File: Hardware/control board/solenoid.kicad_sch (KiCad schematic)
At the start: 8 parts, among them J11 Screw_Terminal_01x02, Q3 NMOS

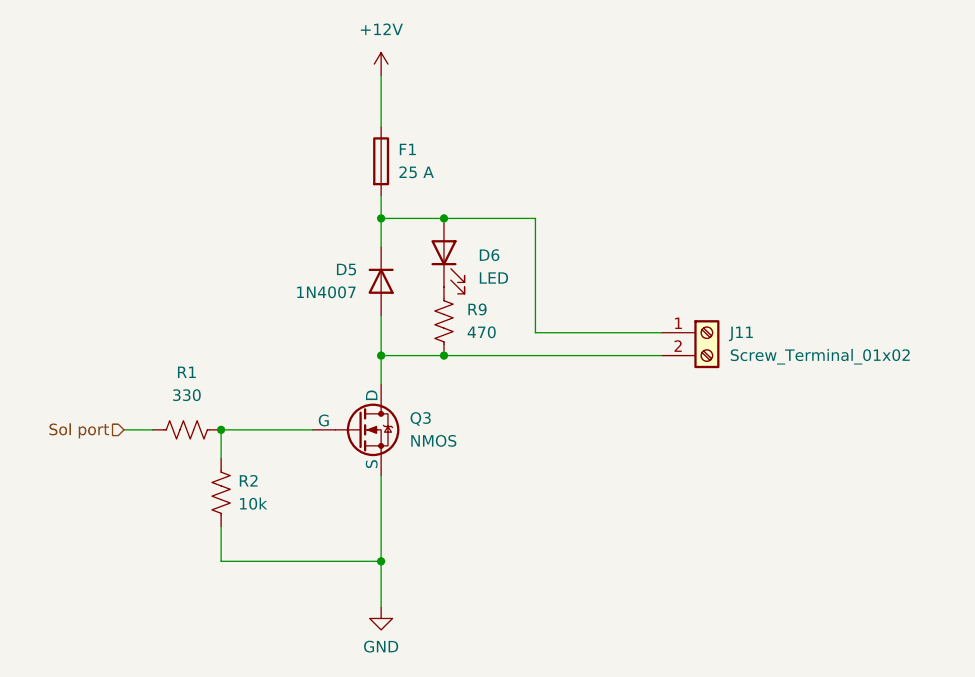
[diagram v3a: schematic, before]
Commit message: updated resistor values for 14.8 V battery
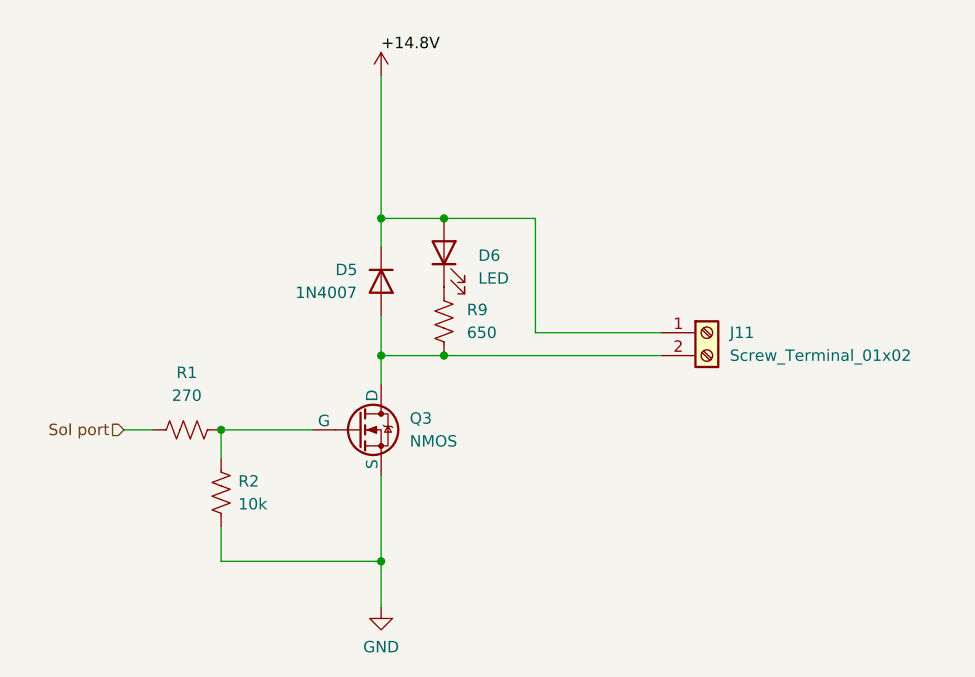
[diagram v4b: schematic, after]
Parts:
- removed F1: 25 A, symbol Device:Fuse
- R1: value 330 -> 270
- R9: value 470 -> 650
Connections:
- net +12V: now also D5.1 (K), D6.2 (A), J11.1 (Pin_1)
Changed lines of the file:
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@@
-    (stroke (width 0) (type default))
-  )
-  (wire (pts (xy 122.555 73.025) (xy 122.555 75.565))
     (stroke (width 0) (type default))
   )
@@
     (stroke (width 0) (type default))
   )
-  (wire (pts (xy 122.555 59.69) (xy 122.555 65.405))
+  (wire (pts (xy 122.555 59.69) (xy 122.555 75.565))
     (stroke (width 0) (type default))
   )
   (wire (pts (xy 139.7 88.265) (xy 153.67 88.265))
     (stroke (width 0) (type default))
+  )
+  (label "+14.8V" (at 122.555 57.15 0) (fields_autoplaced)
+    (effects (font (size 1.27 1.27)) (justify left bottom))
   )
   (hierarchical_label "Sol port" (shape input) (at 93.98 99.06 180) (fields_autoplaced)
@@
     )
   )
-  (symbol (lib_id "Device:Fuse") (at 122.555 69.215 0) (unit 1)
-    (in_bom yes) (on_board yes) (dnp no) (fields_autoplaced)
-    (property "Reference" "F1" (at 124.46 67.945 0)
-      (effects (font (size 1.27 1.27)) (justify left))
-    )
-    (property "Value" "25 A" (at 124.46 70.485 0)
-      (effects (font (size 1.27 1.27)) (justify left))
-    )
-    (property "Footprint" "" (at 120.777 69.215 90)
-      (effects (font (size 1.27 1.27)) hide)
-    )
-    (property "Datasheet" "~" (at 122.555 69.215 0)
-      (effects (font (size 1.27 1.27)) hide)
-    )
-    (pin "1")
-    (pin "2")
-    (instances
-      (project "solenoid"
-        (path "/b4ed5960-473e-41d7-9d87-eb439ed22219"
-          (reference "F1") (unit 1)
-        )
-      )
-      (project "control board"
-        (path "/cf0863a8-7f64-449b-8eb4-3c06c871fb37/9fd0b45f-6f46-40af-ae0d-29c33b45e498"
-          (reference "F1") (unit 1)
-        )
-        (path "/cf0863a8-7f64-449b-8eb4-3c06c871fb37/6163a064-c95f-47b6-9c17-0e18c391c233"
-          (reference "F1") (unit 1)
-        )
-        (path "/cf0863a8-7f64-449b-8eb4-3c06c871fb37/f39ce93b-3626-4dde-a021-b00a2c8134c7"
-          (reference "F1") (unit 1)
-        )
-      )
-    )
-  )
   (symbol (lib_id "Device:LED") (at 129.54 79.375 90) (unit 1)
     (in_bom yes) (on_board yes) (dnp no) (fields_autoplaced)
@@
       (effects (font (size 1.27 1.27)))
     )
-    (property "Value" "330" (at 100.965 95.25 90)
+    (property "Value" "270" (at 100.965 95.25 90)
       (effects (font (size 1.27 1.27)))
     )
@@
       (effects (font (size 1.27 1.27)) (justify left))
     )
-    (property "Value" "470" (at 132.08 88.265 0)
+    (property "Value" "650" (at 132.08 88.265 0)
       (effects (font (size 1.27 1.27)) (justify left))
     )
@@
   )
   (symbol (lib_id "power:+12V") (at 122.555 59.69 0) (unit 1)
-    (in_bom yes) (on_board yes) (dnp no) (fields_autoplaced)
+    (in_bom yes) (on_board yes) (dnp no)
     (property "Reference" "#PWR01" (at 122.555 63.5 0)
       (effects (font (size 1.27 1.27)) hide)
     )
-    (property "Value" "+12V" (at 122.555 54.61 0)
-      (effects (font (size 1.27 1.27)))
+    (property "Value" "+12V" (at 122.555 55.245 0)
+      (effects (font (size 1.27 1.27)) hide)
     )
     (property "Footprint" "" (at 122.555 59.69 0)

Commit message: updated resistor values to use common values
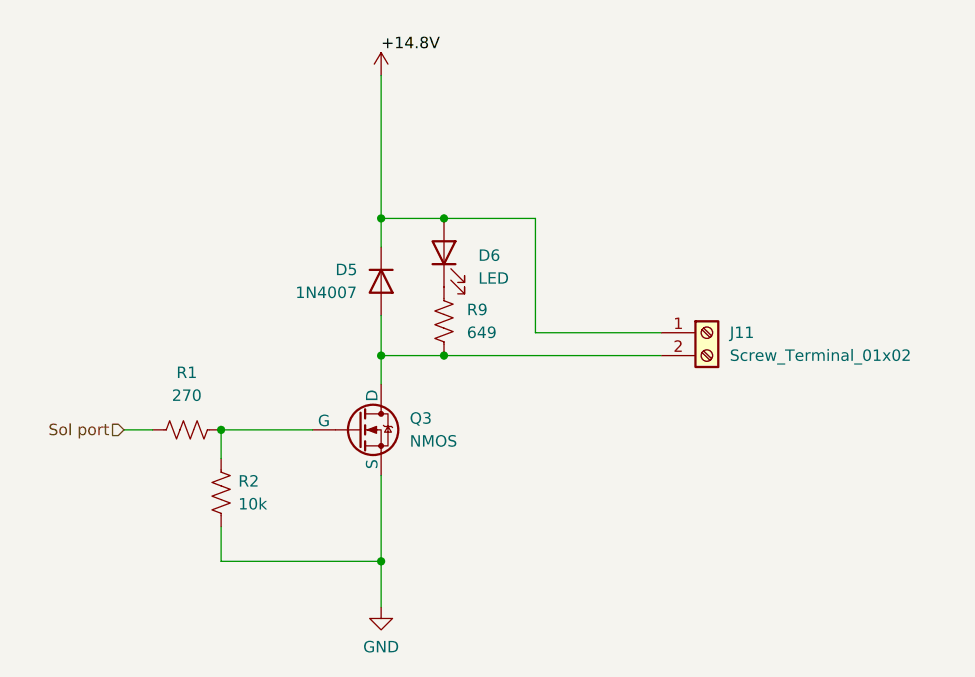
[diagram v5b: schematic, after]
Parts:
- R9: value 650 -> 649
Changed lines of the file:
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@@
       (effects (font (size 1.27 1.27)) (justify left))
     )
-    (property "Value" "650" (at 132.08 88.265 0)
+    (property "Value" "649" (at 132.08 88.265 0)
       (effects (font (size 1.27 1.27)) (justify left))
     )

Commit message: Revert "Merge branch 'hardware' of https://github.com/bruin-underwater-robotics/2023-2024 into hardware"
This reverts commit 2d92dd737ed49dde43700235594c19fac80c6213, reversing
changes made to 7ccd23260c988ead49c0bcfa936e50f6d09a7000.
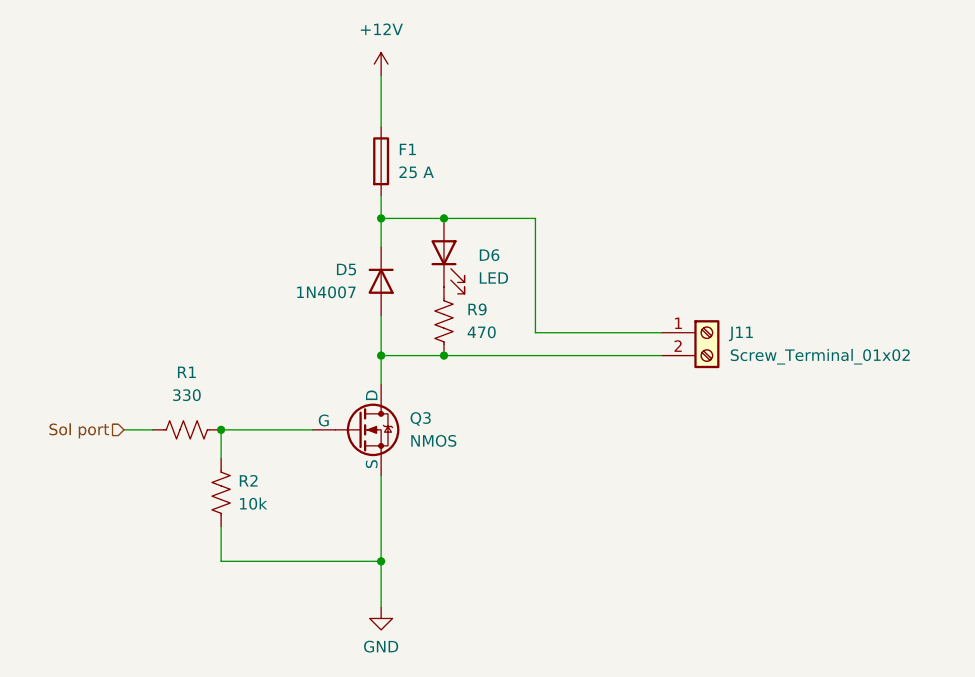
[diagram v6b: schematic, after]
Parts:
- added F1: 25 A, symbol Device:Fuse
- R1: value 270 -> 330
- R9: value 649 -> 470
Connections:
- net +12V: now also F1.1; no longer D5.1 (K), D6.2 (A), J11.1 (Pin_1)
- new net: D5.1 (K), D6.2 (A), F1.2, J11.1 (Pin_1)
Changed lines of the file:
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@@
+    (stroke (width 0) (type default))
+  )
+  (wire (pts (xy 122.555 73.025) (xy 122.555 75.565))
     (stroke (width 0) (type default))
   )
@@
     (stroke (width 0) (type default))
   )
-  (wire (pts (xy 122.555 59.69) (xy 122.555 75.565))
+  (wire (pts (xy 122.555 59.69) (xy 122.555 65.405))
     (stroke (width 0) (type default))
   )
   (wire (pts (xy 139.7 88.265) (xy 153.67 88.265))
     (stroke (width 0) (type default))
-  )
-  (label "+14.8V" (at 122.555 57.15 0) (fields_autoplaced)
-    (effects (font (size 1.27 1.27)) (justify left bottom))
   )
   (hierarchical_label "Sol port" (shape input) (at 93.98 99.06 180) (fields_autoplaced)
@@
     )
   )
+  (symbol (lib_id "Device:Fuse") (at 122.555 69.215 0) (unit 1)
+    (in_bom yes) (on_board yes) (dnp no) (fields_autoplaced)
+    (property "Reference" "F1" (at 124.46 67.945 0)
+      (effects (font (size 1.27 1.27)) (justify left))
+    )
+    (property "Value" "25 A" (at 124.46 70.485 0)
+      (effects (font (size 1.27 1.27)) (justify left))
+    )
+    (property "Footprint" "" (at 120.777 69.215 90)
+      (effects (font (size 1.27 1.27)) hide)
+    )
+    (property "Datasheet" "~" (at 122.555 69.215 0)
+      (effects (font (size 1.27 1.27)) hide)
+    )
+    (pin "1")
+    (pin "2")
+    (instances
+      (project "solenoid"
+        (path "/b4ed5960-473e-41d7-9d87-eb439ed22219"
+          (reference "F1") (unit 1)
+        )
+      )
+      (project "control board"
+        (path "/cf0863a8-7f64-449b-8eb4-3c06c871fb37/9fd0b45f-6f46-40af-ae0d-29c33b45e498"
+          (reference "F1") (unit 1)
+        )
+        (path "/cf0863a8-7f64-449b-8eb4-3c06c871fb37/6163a064-c95f-47b6-9c17-0e18c391c233"
+          (reference "F1") (unit 1)
+        )
+        (path "/cf0863a8-7f64-449b-8eb4-3c06c871fb37/f39ce93b-3626-4dde-a021-b00a2c8134c7"
+          (reference "F1") (unit 1)
+        )
+      )
+    )
+  )
   (symbol (lib_id "Device:LED") (at 129.54 79.375 90) (unit 1)
     (in_bom yes) (on_board yes) (dnp no) (fields_autoplaced)
@@
       (effects (font (size 1.27 1.27)))
     )
-    (property "Value" "270" (at 100.965 95.25 90)
+    (property "Value" "330" (at 100.965 95.25 90)
       (effects (font (size 1.27 1.27)))
     )
@@
       (effects (font (size 1.27 1.27)) (justify left))
     )
-    (property "Value" "649" (at 132.08 88.265 0)
+    (property "Value" "470" (at 132.08 88.265 0)
       (effects (font (size 1.27 1.27)) (justify left))
     )
@@
   )
   (symbol (lib_id "power:+12V") (at 122.555 59.69 0) (unit 1)
-    (in_bom yes) (on_board yes) (dnp no)
+    (in_bom yes) (on_board yes) (dnp no) (fields_autoplaced)
     (property "Reference" "#PWR01" (at 122.555 63.5 0)
       (effects (font (size 1.27 1.27)) hide)
     )
-    (property "Value" "+12V" (at 122.555 55.245 0)
-      (effects (font (size 1.27 1.27)) hide)
+    (property "Value" "+12V" (at 122.555 54.61 0)
+      (effects (font (size 1.27 1.27)))
     )
     (property "Footprint" "" (at 122.555 59.69 0)

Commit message: revised control board design and updated voltage indicators
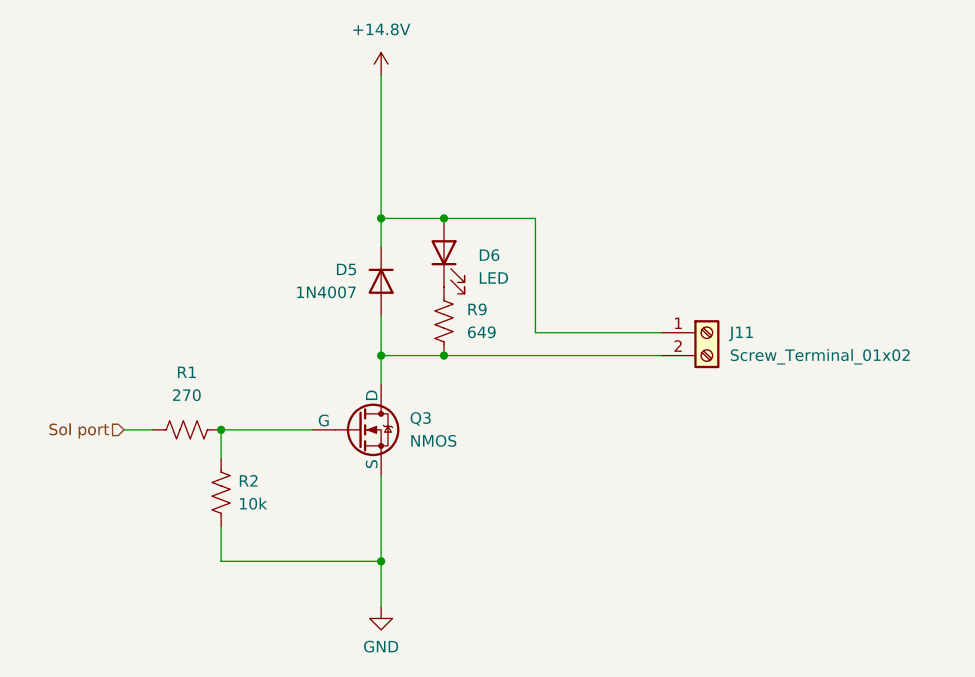
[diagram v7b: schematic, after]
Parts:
- removed F1: 25 A, symbol Device:Fuse
- R1: value 330 -> 270
- R9: value 470 -> 649
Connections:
- net +14.8V: now reaches D5.1 (K), D6.2 (A), J11.1 (Pin_1)
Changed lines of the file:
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@@
-    (stroke (width 0) (type default))
-  )
-  (wire (pts (xy 122.555 73.025) (xy 122.555 75.565))
     (stroke (width 0) (type default))
   )
@@
     (stroke (width 0) (type default))
   )
-  (wire (pts (xy 122.555 59.69) (xy 122.555 65.405))
+  (wire (pts (xy 122.555 59.69) (xy 122.555 75.565))
     (stroke (width 0) (type default))
   )
@@
     )
   )
-  (symbol (lib_id "Device:Fuse") (at 122.555 69.215 0) (unit 1)
-    (in_bom yes) (on_board yes) (dnp no) (fields_autoplaced)
-    (property "Reference" "F1" (at 124.46 67.945 0)
-      (effects (font (size 1.27 1.27)) (justify left))
-    )
-    (property "Value" "25 A" (at 124.46 70.485 0)
-      (effects (font (size 1.27 1.27)) (justify left))
-    )
-    (property "Footprint" "" (at 120.777 69.215 90)
-      (effects (font (size 1.27 1.27)) hide)
-    )
-    (property "Datasheet" "~" (at 122.555 69.215 0)
-      (effects (font (size 1.27 1.27)) hide)
-    )
-    (pin "1")
-    (pin "2")
-    (instances
-      (project "solenoid"
-        (path "/b4ed5960-473e-41d7-9d87-eb439ed22219"
-          (reference "F1") (unit 1)
-        )
-      )
-      (project "control board"
-        (path "/cf0863a8-7f64-449b-8eb4-3c06c871fb37/9fd0b45f-6f46-40af-ae0d-29c33b45e498"
-          (reference "F1") (unit 1)
-        )
-        (path "/cf0863a8-7f64-449b-8eb4-3c06c871fb37/6163a064-c95f-47b6-9c17-0e18c391c233"
-          (reference "F1") (unit 1)
-        )
-        (path "/cf0863a8-7f64-449b-8eb4-3c06c871fb37/f39ce93b-3626-4dde-a021-b00a2c8134c7"
-          (reference "F1") (unit 1)
-        )
-      )
-    )
-  )
   (symbol (lib_id "Device:LED") (at 129.54 79.375 90) (unit 1)
     (in_bom yes) (on_board yes) (dnp no) (fields_autoplaced)
@@
       (effects (font (size 1.27 1.27)))
     )
-    (property "Value" "330" (at 100.965 95.25 90)
+    (property "Value" "270" (at 100.965 95.25 90)
       (effects (font (size 1.27 1.27)))
     )
@@
       (effects (font (size 1.27 1.27)) (justify left))
     )
-    (property "Value" "470" (at 132.08 88.265 0)
+    (property "Value" "649" (at 132.08 88.265 0)
       (effects (font (size 1.27 1.27)) (justify left))
     )
@@
         (path "/cf0863a8-7f64-449b-8eb4-3c06c871fb37/f39ce93b-3626-4dde-a021-b00a2c8134c7"
           (reference "R9") (unit 1)
+        )
+      )
+    )
+  )
+  (symbol (lib_id "power:+12V") (at 122.555 59.69 0) (unit 1)
+    (in_bom yes) (on_board yes) (dnp no) (fields_autoplaced)
+    (property "Reference" "#PWR09" (at 122.555 63.5 0)
+      (effects (font (size 1.27 1.27)) hide)
+    )
+    (property "Value" "+14.8V" (at 122.555 54.61 0)
+      (effects (font (size 1.27 1.27)))
+    )
+    (property "Footprint" "" (at 122.555 59.69 0)
+      (effects (font (size 1.27 1.27)) hide)
+    )
+    (property "Datasheet" "" (at 122.555 59.69 0)
+      (effects (font (size 1.27 1.27)) hide)
+    )
+    (pin "1")
+    (instances
+      (project "control board"
+        (path "/cf0863a8-7f64-449b-8eb4-3c06c871fb37/9fd0b45f-6f46-40af-ae0d-29c33b45e498"
+          (reference "#PWR09") (unit 1)
+        )
+        (path "/cf0863a8-7f64-449b-8eb4-3c06c871fb37/6163a064-c95f-47b6-9c17-0e18c391c233"
+          (reference "#PWR010") (unit 1)
+        )
+        (path "/cf0863a8-7f64-449b-8eb4-3c06c871fb37/f39ce93b-3626-4dde-a021-b00a2c8134c7"
+          (reference "#PWR011") (unit 1)
         )
       )
@@
         )
       )
-    )
-  )
-  (symbol (lib_id "power:+12V") (at 122.555 59.69 0) (unit 1)
-    (in_bom yes) (on_board yes) (dnp no) (fields_autoplaced)
-    (property "Reference" "#PWR01" (at 122.555 63.5 0)
-      (effects (font (size 1.27 1.27)) hide)
-    )
-    (property "Value" "+12V" (at 122.555 54.61 0)
-      (effects (font (size 1.27 1.27)))
-    )
-    (property "Footprint" "" (at 122.555 59.69 0)
-      (effects (font (size 1.27 1.27)) hide)
-    )
-    (property "Datasheet" "" (at 122.555 59.69 0)
-      (effects (font (size 1.27 1.27)) hide)
-    )
-    (pin "1")
-    (instances
-      (project "solenoid"
-        (path "/b4ed5960-473e-41d7-9d87-eb439ed22219"
-          (reference "#PWR01") (unit 1)
-        )
-      )
-      (project "control board"
-        (path "/cf0863a8-7f64-449b-8eb4-3c06c871fb37/9fd0b45f-6f46-40af-ae0d-29c33b45e498"
-          (reference "#PWR01") (unit 1)
-        )
-        (path "/cf0863a8-7f64-449b-8eb4-3c06c871fb37/6163a064-c95f-47b6-9c17-0e18c391c233"
-          (reference "#PWR01") (unit 1)
-        )
-        (path "/cf0863a8-7f64-449b-8eb4-3c06c871fb37/f39ce93b-3626-4dde-a021-b00a2c8134c7"
-          (reference "#PWR01") (unit 1)
-        )
-      )
